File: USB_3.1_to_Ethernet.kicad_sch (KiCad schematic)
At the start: 76 parts, among them J1 RJ45_JK0654219, U1 LAN7801_9JX, U2 93LC56B_SN, U3 KSZ9031RNXCC, Y1 25MHz, Y2 25MHz

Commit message: 1. RGMII routing done - LAN7801 RXD 2.Routing for RGMII - TXD on top layer done, bottom layer remaining 3. source termination resistors 27 ohm removed for RGMII
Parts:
- removed R10, R11, R12, R13, R14, R15, R16, R17, R6, R7, R8, R9: 27R, Resistor_SMD:R_0402_1005Metric, symbol Device:R
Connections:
- net RXD0/MODE0 is gone; now on net RXD0: U3.32 (RXD0/MODE0)
- net RXD1/MODE1 is gone; now on net RXD1: U3.31 (RXD1/MODE1)
- net RXD2/MODE2 is gone; now on net RXD2: U3.28 (RXD2/MODE2)
- net RXD3/MODE3 is gone; now on net RXD3: U3.27 (RXD3/MODE3)
- net RX_DV/CLK125_EN is gone; now on net RX_CTL: U3.33 (RX_DV/CLK125_EN)
- net TX_CTL is gone; now on net GTX_CLK: U1.9 (TX_CTL)
- net TX_EN is gone; now on net TXC: U3.25 (TX_EN)
- net AVDDL: now also C40.1, C41.1, C42.1, C43.1, C44.1, C45.1, C46.1, C47.1, C48.1, C49.1

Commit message: 1.complete routing done 2.Ethernet  MDI differential routing done 3.power and gnd  plane on L2 and L3 completed 4.
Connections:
- net AVDDL: no longer C48.1, C49.1
- net GND: no longer C48.2, C49.2
- net TXRXM_A renamed A_-
- net TXRXM_B renamed B_+
- net B_+: now also J1.4 (MX2+); no longer J1.5 (MX2-)
- net TXRXM_C renamed C_-
- net TXRXM_D renamed D_+
- net D_+: now also U3.10 (TXRXP_D); no longer U3.11 (TXRXM_D)
- net TXRXP_A renamed A_+
- net TXRXP_B renamed B_-
- net B_-: now also J1.5 (MX2-); no longer J1.4 (MX2+)
- net TXRXP_C renamed C_+
- net TXRXP_D renamed D_-
- net D_-: now also U3.11 (TXRXM_D); no longer U3.10 (TXRXP_D)
- new net: C48.1, C49.1
- new net: C48.2, C49.2
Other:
- moved on the sheet: C16, C48, C49
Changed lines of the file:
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@@
 	)
 	(junction
-		(at 270.51 72.39)
-		(diameter 0)
-		(color 0 0 0 0)
-	)
-	(junction
 		(at 261.62 52.07)
 		(diameter 0)
@@
 	)
 	(junction
-		(at 276.86 80.01)
-		(diameter 0)
-		(color 0 0 0 0)
-	)
-	(junction
 		(at 257.81 72.39)
 		(diameter 0)
@@
 	)
 	(junction
-		(at 270.51 80.01)
-		(diameter 0)
-		(color 0 0 0 0)
-	)
-	(junction
 		(at 259.08 33.02)
 		(diameter 0)
@@
 	)
 	(junction
-		(at 276.86 72.39)
-		(diameter 0)
-		(color 0 0 0 0)
-	)
-	(junction
 		(at 38.1 134.62)
 		(diameter 0)
@@
 	(wire
 		(pts
-			(xy 156.21 173.99) (xy 151.13 173.99)
+			(xy 154.94 173.99) (xy 151.13 173.99)
 		)
 		(stroke
@@
 	(wire
 		(pts
-			(xy 175.26 140.97) (xy 173.99 140.97)
-		)
-		(stroke
-			(width 0)
-			(type default)
-		)
-	)
-	(wire
-		(pts
 			(xy 264.16 80.01) (xy 270.51 80.01)
 		)
@@
 	(wire
 		(pts
-			(xy 166.37 140.97) (xy 151.13 140.97)
+			(xy 167.64 140.97) (xy 151.13 140.97)
 		)
 		(stroke
@@
 	(wire
 		(pts
-			(xy 276.86 72.39) (xy 283.21 72.39)
+			(xy 271.78 54.61) (xy 278.13 54.61)
 		)
 		(stroke
@@
 	(wire
 		(pts
-			(xy 270.51 72.39) (xy 276.86 72.39)
-		)
-		(stroke
-			(width 0)
-			(type default)
-		)
-	)
-	(wire
-		(pts
 			(xy 246.38 44.45) (xy 248.92 44.45)
 		)
@@
 	(wire
 		(pts
-			(xy 270.51 80.01) (xy 276.86 80.01)
-		)
-		(stroke
-			(width 0)
-			(type default)
-		)
-	)
-	(wire
-		(pts
 			(xy 189.23 38.1) (xy 185.42 38.1)
 		)
@@
 	(wire
 		(pts
-			(xy 276.86 80.01) (xy 283.21 80.01)
+			(xy 271.78 62.23) (xy 278.13 62.23)
 		)
 		(stroke
@@
 		)
 	)
-	(label "TXRXP_C"
+	(label "C_+"
 		(at 123.19 80.01 180)
 		(effects
@@
 		)
 	)
-	(label "TXRXP_D"
+	(label "D_-"
 		(at 154.94 143.51 0)
 		(effects
@@
 		)
 	)
-	(label "TXRXP_A"
-		(at 123.19 69.85 180)
-		(effects
-			(font
-				(size 1.27 1.27)
-			)
-			(justify right bottom)
-		)
-	)
 	(label "CLK"
 		(at 34.29 172.72 180)
@@
 		)
 	)
-	(label "TXRXM_D"
+	(label "D_+"
 		(at 154.94 138.43 0)
 		(effects
@@
 		)
 	)
-	(label "TXRXP_D"
+	(label "D_+"
 		(at 123.19 85.09 180)
 		(effects
@@
 		)
 	)
-	(label "TXRXP_A"
-		(at 156.21 173.99 0)
+	(label "A_+"
+		(at 154.94 173.99 0)
 		(effects
 			(font
@@
 		)
 	)
-	(label "TXRXP_B"
+	(label "B_-"
 		(at 123.19 74.93 180)
 		(effects
@@
 		)
 	)
-	(label "TXRXM_B"
+	(label "B_-"
 		(at 154.94 158.75 0)
 		(effects
@@
 		)
 	)
-	(label "TXRXM_A"
+	(label "A_-"
 		(at 154.94 168.91 0)
 		(effects
@@
 		)
 	)
-	(label "TXRXM_A"
-		(at 123.19 72.39 180)
+	(label "~{RESET_N}"
+		(at 24.13 40.64 180)
 		(effects
 			(font
@@
 		)
 	)
-	(label "~{RESET_N}"
-		(at 24.13 40.64 180)
+	(label "A_+"
+		(at 123.19 69.85 180)
 		(effects
 			(font
@@
 		)
 	)
-	(label "TXRXP_B"
+	(label "B_+"
 		(at 154.94 163.83 0)
 		(effects
@@
 		)
 	)
-	(label "TXRXM_C"
+	(label "C_-"
 		(at 123.19 82.55 180)
 		(effects
@@
 		)
 	)
-	(label "TXRXP_C"
+	(label "C_+"
 		(at 154.94 153.67 0)
 		(effects
@@
 		)
 	)
+	(label "A_-"
+		(at 123.19 72.39 180)
+		(effects
+			(font
+				(size 1.27 1.27)
+			)
+			(justify right bottom)
+		)
+	)
 	(label "GTX_CLK"
 		(at 120.65 41.91 180)
@@
 		)
 	)
-	(label "TXRXM_D"
+	(label "D_-"
 		(at 123.19 87.63 180)
 		(effects
@@
 		)
 	)
-	(label "TXRXM_C"
+	(label "C_-"
 		(at 154.94 148.59 0)
 		(effects
@@
 		)
 	)
-	(label "TXRXM_B"
+	(label "B_+"
 		(at 123.19 77.47 180)
 		(effects
@@
 		)
 		(property "Value" "0.1uF"
-			(at 167.386 172.72 90)
+			(at 167.64 172.72 90)
 			(show_name no)
 			(do_not_autoplace no)
@@
 	(symbol
 		(lib_id "Device:C")
-		(at 276.86 76.2 0)
+		(at 271.78 58.42 0)
 		(unit 1)
 		(body_style 1)
@@
 		(dnp no)
 		(property "Reference" "C48"
-			(at 277.114 73.914 0)
+			(at 272.034 56.134 0)
 			(show_name no)
 			(do_not_autoplace no)
@@
 		)
 		(property "Value" "0.1uF"
-			(at 276.86 78.74 0)
+			(at 271.78 60.96 0)
 			(show_name no)
 			(do_not_autoplace no)
@@
 		)
 		(property "Footprint" "Capacitor_SMD:C_01005_0402Metric"
-			(at 277.8252 80.01 0)
+			(at 272.7452 62.23 0)
 			(hide yes)
 			(show_name no)
@@
 		)
 		(property "Datasheet" ""
-			(at 276.86 76.2 0)
+			(at 271.78 58.42 0)
 			(hide yes)
 			(show_name no)
@@
 		)
 		(property "Description" "Unpolarized capacitor"
-			(at 276.86 76.2 0)
+			(at 271.78 58.42 0)
 			(hide yes)
 			(show_name no)
@@
 	(symbol
 		(lib_id "Device:C")
-		(at 283.21 76.2 0)
+		(at 278.13 58.42 0)
 		(unit 1)
 		(body_style 1)
@@
 		(dnp no)
 		(property "Reference" "C49"
-			(at 283.464 73.914 0)
+			(at 278.384 56.134 0)
 			(show_name no)
 			(do_not_autoplace no)
@@
 		)
 		(property "Value" "0.1uF"
-			(at 283.718 78.74 0)
+			(at 278.638 60.96 0)
 			(show_name no)
 			(do_not_autoplace no)
@@
 		)
 		(property "Footprint" "Capacitor_SMD:C_01005_0402Metric"
-			(at 284.1752 80.01 0)
+			(at 279.0952 62.23 0)
 			(hide yes)
 			(show_name no)
@@
 		)
 		(property "Datasheet" ""
-			(at 283.21 76.2 0)
+			(at 278.13 58.42 0)
 			(hide yes)
 			(show_name no)
@@
 		)
 		(property "Description" "Unpolarized capacitor"
-			(at 283.21 76.2 0)
+			(at 278.13 58.42 0)
 			(hide yes)
 			(show_name no)
@@
 	(symbol
 		(lib_id "Device:C")
-		(at 170.18 140.97 270)
+		(at 171.45 140.97 270)
 		(unit 1)
 		(body_style 1)
@@
 		(dnp no)
 		(property "Reference" "C16"
-			(at 173.736 142.494 90)
+			(at 175.006 142.494 90)
 			(show_name no)
 			(do_not_autoplace no)
@@
 		)
 		(property "Value" "0.1uF"
-			(at 166.116 142.24 90)
+			(at 167.386 142.24 90)
 			(show_name no)
 			(do_not_autoplace no)
@@
 		)
 		(property "Footprint" "Capacitor_SMD:C_0402_1005Metric"
-			(at 166.37 141.9352 0)
+			(at 167.64 141.9352 0)
 			(hide yes)
 			(show_name no)
@@
 		)
 		(property "Datasheet" ""
-			(at 170.18 140.97 0)
+			(at 171.45 140.97 0)
 			(hide yes)
 			(show_name no)
@@
 		)
 		(property "Description" "Unpolarized capacitor"
-			(at 170.18 140.97 0)
+			(at 171.45 140.97 0)
 			(hide yes)
 			(show_name no)

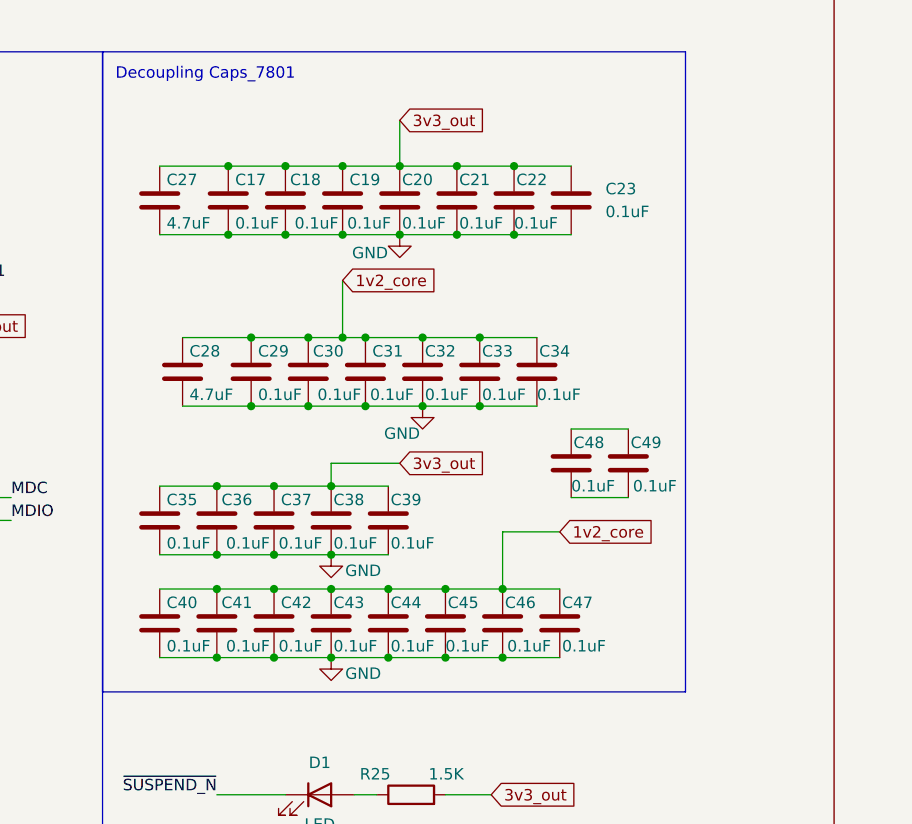
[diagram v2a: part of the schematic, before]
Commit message: microadjustments  in via connections of  gnd
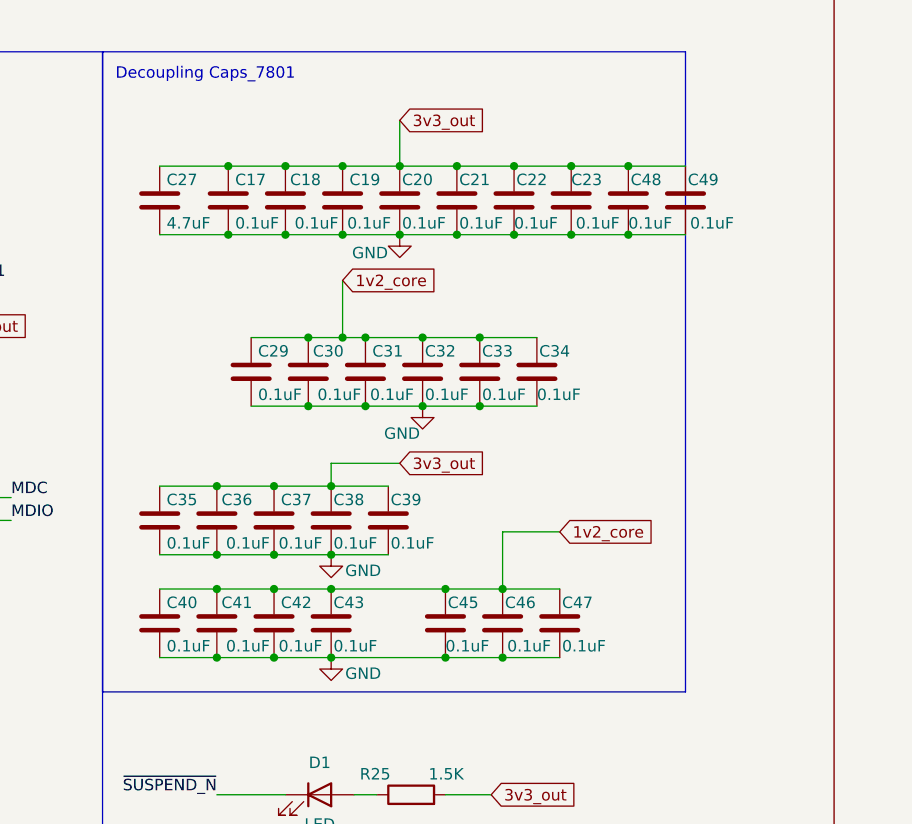
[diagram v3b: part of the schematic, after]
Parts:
- removed C28: 4.7uF, Capacitor_SMD:C_01005_0402Metric, symbol Device:C
- removed C44: 0.1uF, Capacitor_SMD:C_01005_0402Metric, symbol Device:C
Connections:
- net AVDDH: now also C48.1, C49.1
- net GND: now also C48.2, C49.2
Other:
- moved on the sheet: C48, C49
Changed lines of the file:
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@@
 	)
 	(junction
-		(at 252.73 33.02)
+		(at 278.13 25.4)
 		(diameter 0)
 		(color 0 0 0 0)
 	)
 	(junction
-		(at 245.11 60.96)
+		(at 271.78 33.02)
 		(diameter 0)
 		(color 0 0 0 0)
 	)
 	(junction
-		(at 242.57 52.07)
+		(at 252.73 33.02)
 		(diameter 0)
 		(color 0 0 0 0)
 	)
 	(junction
-		(at 236.22 44.45)
+		(at 245.11 60.96)
 		(diameter 0)
 		(color 0 0 0 0)
 	)
 	(junction
-		(at 252.73 25.4)
+		(at 242.57 52.07)
 		(diameter 0)
 		(color 0 0 0 0)
 	)
 	(junction
-		(at 265.43 33.02)
+		(at 252.73 25.4)
 		(diameter 0)
 		(color 0 0 0 0)
 	)
 	(junction
-		(at 240.03 25.4)
+		(at 265.43 33.02)
 		(diameter 0)
 		(color 0 0 0 0)
 	)
 	(junction
-		(at 205.74 64.77)
+		(at 240.03 25.4)
 		(diameter 0)
 		(color 0 0 0 0)
 	)
 	(junction
-		(at 236.22 52.07)
+		(at 205.74 64.77)
 		(diameter 0)
 		(color 0 0 0 0)
@@
 	)
 	(junction
-		(at 251.46 80.01)
+		(at 238.76 80.01)
 		(diameter 0)
 		(color 0 0 0 0)
 	)
 	(junction
-		(at 238.76 80.01)
+		(at 261.62 52.07)
 		(diameter 0)
 		(color 0 0 0 0)
 	)
 	(junction
-		(at 261.62 52.07)
+		(at 271.78 25.4)
 		(diameter 0)
 		(color 0 0 0 0)
@@
 	)
 	(junction
-		(at 251.46 72.39)
-		(diameter 0)
-		(color 0 0 0 0)
-	)
-	(junction
 		(at 82.55 124.46)
 		(diameter 0)
@@
 	)
 	(junction
+		(at 278.13 33.02)
+		(diameter 0)
+		(color 0 0 0 0)
+	)
+	(junction
 		(at 38.1 134.62)
 		(diameter 0)
@@
 	(wire
 		(pts
-			(xy 251.46 72.39) (xy 257.81 72.39)
+			(xy 271.78 33.02) (xy 278.13 33.02)
 		)
 		(stroke
@@
 	(wire
 		(pts
+			(xy 271.78 25.4) (xy 278.13 25.4)
+		)
+		(stroke
+			(width 0)
+			(type default)
+		)
+	)
+	(wire
+		(pts
 			(xy 26.67 45.72) (xy 27.94 45.72)
 		)
@@
 	(wire
 		(pts
-			(xy 228.6 44.45) (xy 236.22 44.45)
-		)
-		(stroke
-			(width 0)
-			(type default)
-		)
-	)
-	(wire
-		(pts
 			(xy 147.32 193.04) (xy 152.4 193.04)
 		)
@@
 	(wire
 		(pts
-			(xy 245.11 72.39) (xy 251.46 72.39)
+			(xy 245.11 72.39) (xy 257.81 72.39)
 		)
 		(stroke
@@
 	(wire
 		(pts
-			(xy 245.11 80.01) (xy 251.46 80.01)
+			(xy 245.11 80.01) (xy 257.81 80.01)
 		)
 		(stroke
@@
 	(wire
 		(pts
-			(xy 251.46 80.01) (xy 257.81 80.01)
-		)
-		(stroke
-			(width 0)
-			(type default)
-		)
-	)
-	(wire
-		(pts
 			(xy 120.65 52.07) (xy 128.27 52.07)
 		)
@@
 	(wire
 		(pts
-			(xy 271.78 54.61) (xy 278.13 54.61)
+			(xy 278.13 25.4) (xy 284.48 25.4)
 		)
 		(stroke
@@
 	(wire
 		(pts
-			(xy 228.6 52.07) (xy 236.22 52.07)
-		)
-		(stroke
-			(width 0)
-			(type default)
-		)
-	)
-	(wire
-		(pts
 			(xy 24.13 143.51) (xy 38.1 143.51)
 		)
@@
 	(wire
 		(pts
-			(xy 271.78 62.23) (xy 278.13 62.23)
+			(xy 278.13 33.02) (xy 284.48 33.02)
 		)
 		(stroke
@@
 	(symbol
 		(lib_id "Device:C")
-		(at 271.78 58.42 0)
+		(at 278.13 29.21 0)
 		(unit 1)
 		(body_style 1)
@@
 		(dnp no)
 		(property "Reference" "C48"
-			(at 272.034 56.134 0)
+			(at 278.384 26.924 0)
 			(show_name no)
 			(do_not_autoplace no)
@@
 		)
 		(property "Value" "0.1uF"
-			(at 271.78 60.96 0)
+			(at 278.13 31.75 0)
 			(show_name no)
 			(do_not_autoplace no)
@@
 		)
 		(property "Footprint" "Capacitor_SMD:C_01005_0402Metric"
-			(at 272.7452 62.23 0)
+			(at 279.0952 33.02 0)
 			(hide yes)
 			(show_name no)
@@
 		)
 		(property "Datasheet" ""
-			(at 271.78 58.42 0)
+			(at 278.13 29.21 0)
 			(hide yes)
 			(show_name no)
@@
 		)
 		(property "Description" "Unpolarized capacitor"
-			(at 271.78 58.42 0)
+			(at 278.13 29.21 0)
 			(hide yes)
 			(show_name no)
@@
 	(symbol
 		(lib_id "Device:C")
-		(at 278.13 58.42 0)
+		(at 284.48 29.21 0)
 		(unit 1)
 		(body_style 1)
@@
 		(dnp no)
 		(property "Reference" "C49"
-			(at 278.384 56.134 0)
+			(at 284.734 26.924 0)
 			(show_name no)
 			(do_not_autoplace no)
@@
 		)
 		(property "Value" "0.1uF"
-			(at 278.638 60.96 0)
+			(at 284.988 31.75 0)
 			(show_name no)
 			(do_not_autoplace no)
@@
 		)
 		(property "Footprint" "Capacitor_SMD:C_01005_0402Metric"
-			(at 279.0952 62.23 0)
+			(at 285.4452 33.02 0)
 			(hide yes)
 			(show_name no)
@@
 		)
 		(property "Datasheet" ""
-			(at 278.13 58.42 0)
+			(at 284.48 29.21 0)
 			(hide yes)
 			(show_name no)
@@
 		)
 		(property "Description" "Unpolarized capacitor"
-			(at 278.13 58.42 0)
+			(at 284.48 29.21 0)
 			(hide yes)
 			(show_name no)
@@
 		(in_pos_files yes)
 		(dnp no)
-		(fields_autoplaced yes)
 		(property "Reference" "C23"
-			(at 275.59 27.9399 0)
+			(at 271.78 26.924 0)
 			(show_name no)
 			(do_not_autoplace no)
@@
 		)
 		(property "Value" "0.1uF"
-			(at 275.59 30.4799 0)
+			(at 272.288 31.75 0)
 			(show_name no)
 			(do_not_autoplace no)
@@
 	(symbol
 		(lib_id "Device:C")
-		(at 251.46 76.2 0)
-		(unit 1)
-		(body_style 1)
-		(exclude_from_sim no)
-		(in_bom yes)
-		(on_board yes)
-		(in_pos_files yes)
-		(dnp no)
-		(property "Reference" "C44"
-			(at 251.714 73.914 0)
-			(show_name no)
-			(do_not_autoplace no)
-			(effects
-				(font
-					(size 1.27 1.27)
-				)
-				(justify left)
-			)
-		)
-		(property "Value" "0.1uF"
-			(at 251.714 78.74 0)
-			(show_name no)
-			(do_not_autoplace no)
-			(effects
-				(font
-					(size 1.27 1.27)
-				)
-				(justify left)
-			)
-		)
-		(property "Footprint" "Capacitor_SMD:C_01005_0402Metric"
-			(at 252.4252 80.01 0)
-			(hide yes)
-			(show_name no)
-			(do_not_autoplace no)
-			(effects
-				(font
-					(size 1.27 1.27)
-				)
-			)
-		)
-		(property "Datasheet" ""
-			(at 251.46 76.2 0)
-			(hide yes)
-			(show_name no)
-			(do_not_autoplace no)
-			(effects
-				(font
-					(size 1.27 1.27)
-				)
-			)
-		)
-		(property "Description" "Unpolarized capacitor"
-			(at 251.46 76.2 0)
-			(hide yes)
-			(show_name no)
-			(do_not_autoplace no)
-			(effects
-				(font
-					(size 1.27 1.27)
-				)
-			)
-		)
-		(pin "1"
-		)
-		(pin "2"
-		)
-		(instances
-			(project "USB_3.1_to_Ethernet"
-				(path "/b00c1253-ab18-4b3e-8546-134ebc6e3f42"
-					(reference "C44")
-					(unit 1)
-				)
-			)
-		)
-	)
-	(symbol
-		(lib_id "Device:C")
 		(at 246.38 29.21 0)
 		(unit 1)
@@
 					(unit 1)
 				)
-			)
-		)
-	)
-	(symbol
-		(lib_id "Device:C")
-		(at 228.6 48.26 0)
-		(unit 1)
-		(body_style 1)
-		(exclude_from_sim no)
-		(in_bom yes)
-		(on_board yes)
-		(in_pos_files yes)
-		(dnp no)
-		(property "Reference" "C28"
-			(at 229.362 45.974 0)
-			(show_name no)
-			(do_not_autoplace no)
-			(effects
-				(font
-					(size 1.27 1.27)
-				)
-				(justify left)
-			)
-		)
-		(property "Value" "4.7uF"
-			(at 229.362 50.8 0)
-			(show_name no)
-			(do_not_autoplace no)
-			(effects
-				(font
-					(size 1.27 1.27)
-				)
-				(justify left)
-			)
-		)
-		(property "Footprint" "Capacitor_SMD:C_01005_0402Metric"
-			(at 229.5652 52.07 0)
-			(hide yes)
-			(show_name no)
-			(do_not_autoplace no)
-			(effects
-				(font
-					(size 1.27 1.27)
-				)
-			)
-		)
-		(property "Datasheet" ""
-			(at 228.6 48.26 0)
-			(hide yes)
-			(show_name no)
-			(do_not_autoplace no)
-			(effects
-				(font
-					(size 1.27 1.27)
-				)
-			)
-		)
-		(property "Description" "Unpolarized capacitor"
-			(at 228.6 48.26 0)
-			(hide yes)
-			(show_name no)
-			(do_not_autoplace no)
-			(effects
-				(font
-					(size 1.27 1.27)
-				)
-			)
-		)
-		(pin "1"
-		)
-		(pin "2"
-		)
-		(instances
-			(project "USB_3.1_to_Ethernet"
-				(path "/b00c1253-ab18-4b3e-8546-134ebc6e3f42"
-					(reference "C28")
-					(unit 1)
-				)
